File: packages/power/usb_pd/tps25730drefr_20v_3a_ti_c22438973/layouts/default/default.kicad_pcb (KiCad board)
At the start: 2 copper layers, 12 parts

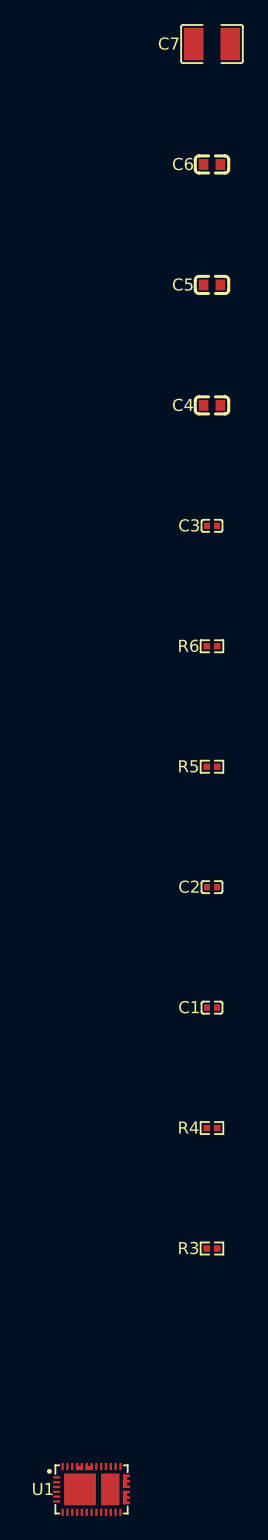
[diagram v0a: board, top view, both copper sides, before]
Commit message: Align the USB-PD sink front end with the TPS25730 reference design
Update the TPS25730DREFR package so the receptacle-facing VBUS capacitance matches TI's recommended CVBUS window while the switched PPHV side carries the larger bulk energy store recommended for the integrated sink path. The package also stops adding local I2C pullups so a downstream shared bus can own pullup sizing explicitly.

Constraint: USB-facing sink capacitance should stay inside the stricter Type-C-facing VBUS guidance while the TPS25730D still needs its recommended board capacitances
Constraint: Repository packages must keep explicit LCSC-backed parts and verify with ato
Rejected: Keep 22 uF directly on usb_vbus | exceeds TI's nominal CVBUS recommendation and is harder to defend against Type-C-facing capacitance limits
Rejected: Keep onboard 3.3 kΩ I2C pullups because TI's example shows them | downstream systems may already provide bus pullups and the user explicitly requested removal
Confidence: high
Scope-risk: narrow
Reversibility: clean
Directive: If this package is later paired with a connector-level block, keep USB-facing VBUS capacitance and shared I2C pullups owned by the full system, not duplicated here
Tested: ato --non-interactive build (default and example) in packages/power/usb_pd/tps25730drefr_20v_3a_ti_c22438973
Not-tested: Bench validation against a real USB-PD source and shared external I2C bus
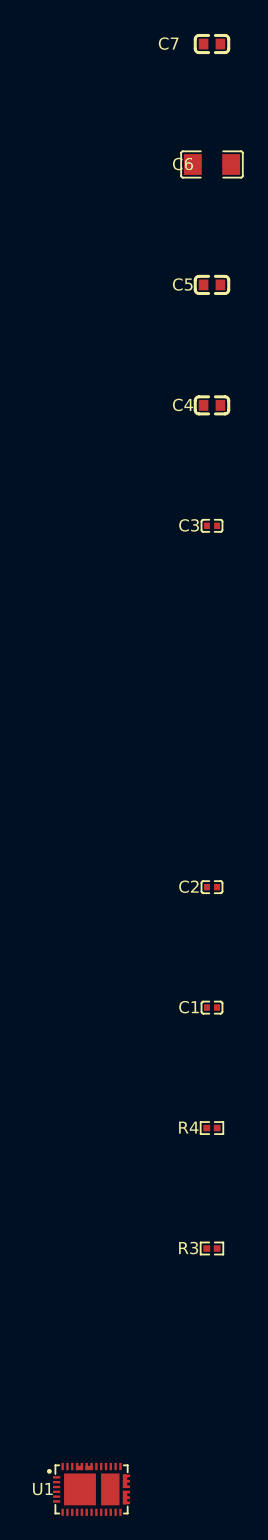
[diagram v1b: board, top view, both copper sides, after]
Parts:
- removed R5, R6: 3.3kΩ ±1%, YAGEO_RC0402FR_073K3L:R0402
- C6: value 10µF ±10% -> 47µF ±20%; footprint Murata_Electronics_GRM188R61E106KA73D:C0603 -> Murata_Electronics_GRM31CR61E476ME44L:C1206
- C7: value 22µF ±10% -> 4.7µF ±10%; footprint Murata_Electronics_GRM32ER71E226KE15L:C1210 -> Murata_Electronics_GRM188R61E475KE11D:C0603

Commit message: Wip TPS25730
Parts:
- removed C6: 47µF ±20%, Murata_Electronics_GRM31CR61E476ME44L:C1206
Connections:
- net sink_vbus_bulk-power-hv renamed sink_vbus-hv

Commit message: Keep the USB-PD sink package deterministic and schematic-friendly
The package now uses explicit local passive part modules again, drops the
unnecessary package-level sink output capacitor, and forces readable net
names for the exposed rails and key internal strap nets. The resulting
layout outputs stay aligned with the package contract while avoiding the
opaque auto-generated net labels that made the schematic harder to use.

Constraint: Package must build with the current atopile CLI in this repo
Constraint: Concrete BOM choices must remain explicit and LCSC-traceable
Rejected: Keep generic passives in source | part-picking path was less deterministic and previously hit flaky EasyEDA resolution
Rejected: Keep unnamed/internal auto-generated nets | violated repo guidance for readable schematic nets
Confidence: high
Scope-risk: narrow
Reversibility: clean
Directive: Preserve explicit net-name overrides for USB_VBUS, SINK_VBUS, 3V3, GND, CC1, CC2, and PD_LIMIT_SEL unless you verify the generated schematic names remain readable without them
Tested:  in packages/power/usb_pd/tps25730drefr_20v_3a_ti_c22438973 (default and example targets passed)
Not-tested: Downstream integration inside a larger design using this package
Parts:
- C1, C2: value 330pF ±5% -> (none)
- C3, C7: value 4.7µF ±10% -> (none)
- C4, C5: value 10µF ±10% -> (none)
- R3: value 10kΩ ±1% -> (none)
- R4: value 200kΩ ±1% -> (none)
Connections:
- net 7 renamed PD_LIMIT_SEL
- net cc1_filter-power-hv renamed CC1
- net cc2_filter-power-hv renamed CC2
- net hv renamed LDO_3V3
- net ldo_1v5_bypass-power-hv renamed LDO_1V5
- net logic_3v3_bypass-power-hv renamed 3V3
- net lv renamed GND
- net sink_vbus-hv renamed SINK_VBUS
- net usb_vbus_bulk-power-hv renamed USB_VBUS
